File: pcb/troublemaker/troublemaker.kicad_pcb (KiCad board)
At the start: 2 copper layers, 419 x 394 mm, 116 parts, among them IC1 TEENSY_4.1, J1 neopixel_data_RPI19_GPIO10, J2 taptempo_led_RPI16_GPIO23, J3 5V_RPI2_OR_4, J4 GND_RPI34, J5 Conn_01x12, SW1 sw_eq2, SW10 sw_grain_playback, SW11 btn_sampler_stop, SW2 sw_eq1, SW3 sw_sub, SW4 sw_bass, SW5 sw_mid, SW6 sw_high, SW7 btn_delay_taptempo, SW8 sw_delay_type, SW9 sw_grain_type, U1 RASPBERRY_PI_4B_4GB, U2 CD74HC4067M, U3 CD74HC4067M, U4 CD74HC4067M, U5 CD74HC4067M, U6 CD74HC4067M

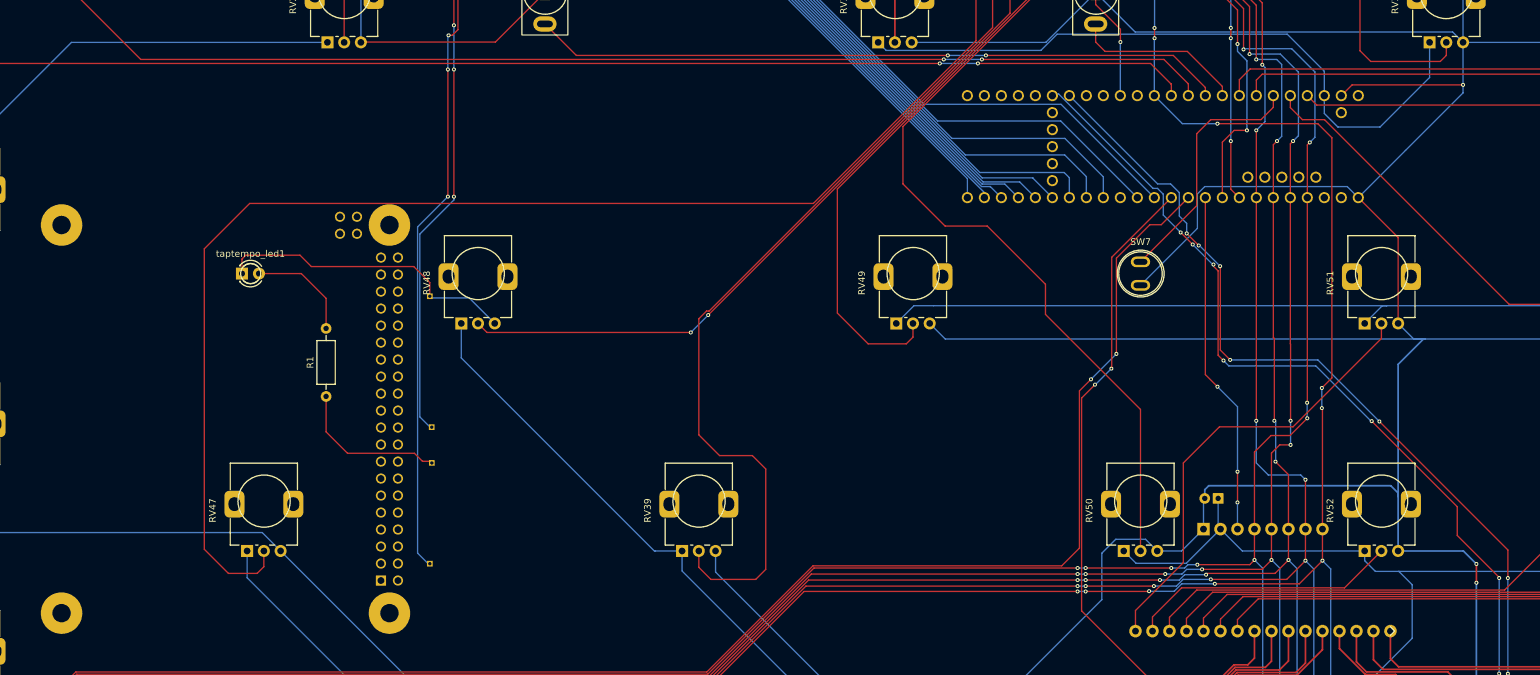
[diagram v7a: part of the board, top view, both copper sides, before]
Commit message: Fixed DRC errors
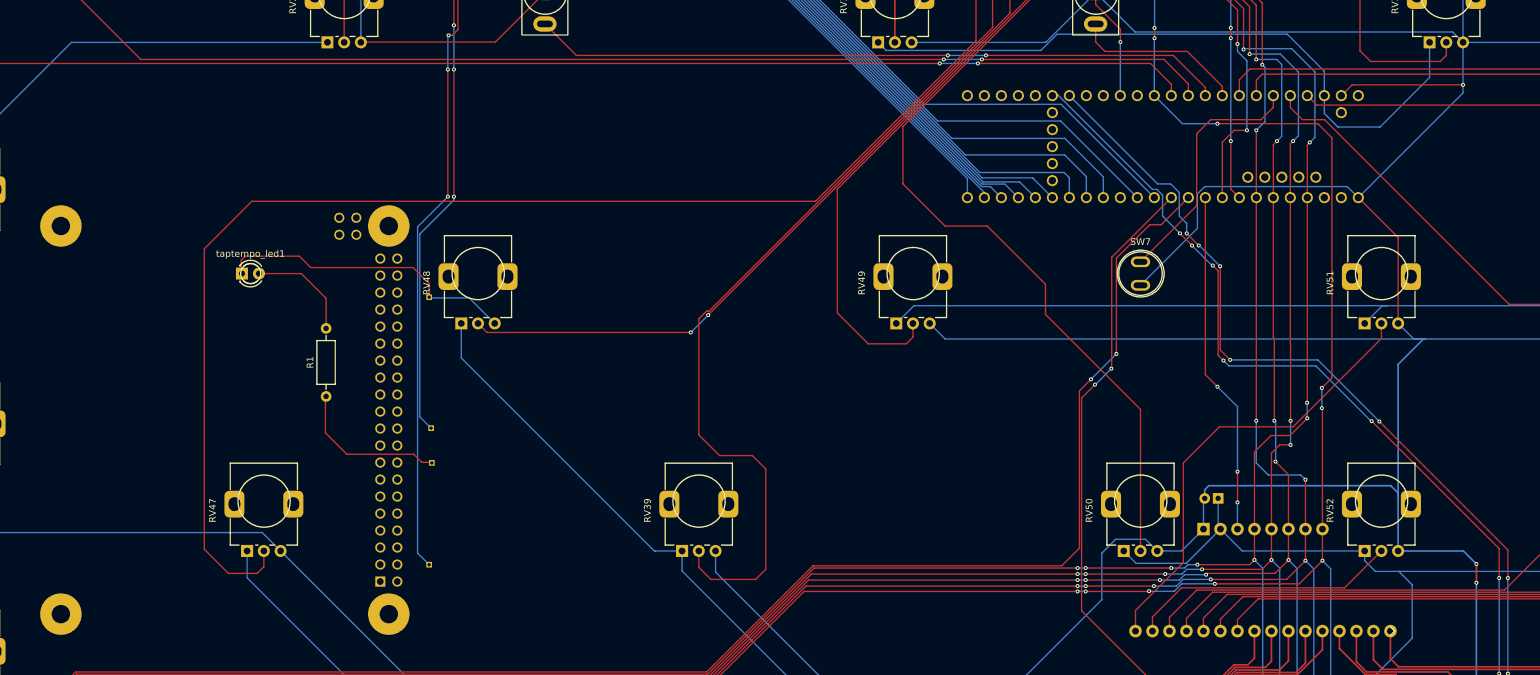
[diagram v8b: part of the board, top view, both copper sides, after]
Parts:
- moved U1 0.18 mm to (143.7, 233.6)
- moved J1 0.18 mm to (174.5, 244.8)
- moved J4 0.18 mm to (174.2, 225.2)
- moved J3 0.18 mm to (174.2, 265.2)
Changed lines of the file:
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@@
 	(footprint "Connector_PinHeader_1.00mm:PinHeader_1x01_P1.00mm_Vertical"
 		(layer "B.Cu")
-		(at 174.587699 244.652048 90)
+		(at 174.487699 244.8 90)
 		(descr "Through hole straight pin header, 1x01, 1.00mm pitch, single row")
 		(tags "Through hole pin header THT 1x01 1.00mm single row")
@@
 	(footprint "Connector_PinHeader_1.00mm:PinHeader_1x01_P1.00mm_Vertical"
 		(layer "B.Cu")
-		(at 174.300199 225.08525 90)
+		(at 174.200199 225.233202 90)
 		(descr "Through hole straight pin header, 1x01, 1.00mm pitch, single row")
 		(tags "Through hole pin header THT 1x01 1.00mm single row")
@@
 	(footprint "RASPBERRY_PI_4B_4GB:MODULE_RASPBERRY_PI_4B_4GB"
 		(layer "B.Cu")
-		(at 143.77 233.442048 90)
+		(at 143.67 233.59 90)
 		(property "Reference" "U1"
 			(at -39.575 29.635 -90)
@@
 	(footprint "Connector_PinHeader_1.00mm:PinHeader_1x01_P1.00mm_Vertical"
 		(layer "B.Cu")
-		(at 174.3 265.052048 90)
+		(at 174.2 265.2 90)
 		(descr "Through hole straight pin header, 1x01, 1.00mm pitch, single row")
 		(tags "Through hole pin header THT 1x01 1.00mm single row")
@@
 	)
 	(gr_text "USB C POWER THIS SIDE"
-		(at 113.800199 266.68525 -90)
+		(at 113.700199 266.833202 -90)
 		(layer "B.Fab")
 		(effects
@@
 	)
 	(segment
-		(start 156.6 220.652048)
-		(end 171.9 220.652048)
+		(start 156.5 220.8)
+		(end 171.8 220.8)
 		(width 0.2)
 		(layer "F.Cu")
@@
 	)
 	(segment
-		(start 146.225 219.527048)
-		(end 146.8 218.952048)
+		(start 146.125 219.675)
+		(end 146.7 219.1)
 		(width 0.2)
 		(layer "F.Cu")
@@
 	)
 	(segment
-		(start 146.225 221.452048)
-		(end 146.225 219.527048)
+		(start 146.125 221.6)
+		(end 146.125 219.675)
 		(width 0.2)
 		(layer "F.Cu")
@@
 	)
 	(segment
-		(start 154.9 218.952048)
-		(end 156.6 220.652048)
+		(start 154.8 219.1)
+		(end 156.5 220.8)
 		(width 0.2)
 		(layer "F.Cu")
@@
 	)
 	(segment
-		(start 146.8 218.952048)
-		(end 154.9 218.952048)
+		(start 146.7 219.1)
+		(end 154.8 219.1)
 		(width 0.2)
 		(layer "F.Cu")
@@
 	)
 	(segment
-		(start 174.300199 223.052247)
-		(end 174.300199 225.08525)
+		(start 174.200199 223.200199)
+		(end 174.200199 225.233202)
 		(width 0.2)
 		(layer "F.Cu")
@@
 	)
 	(segment
-		(start 171.9 220.652048)
-		(end 174.300199 223.052247)
+		(start 171.8 220.8)
+		(end 174.200199 223.200199)
 		(width 0.2)
 		(layer "F.Cu")
@@
 	)
 	(segment
+		(start 255.917753 186.917753)
+		(end 255.917753 172.017753)
+		(width 0.2)
+		(layer "F.Cu")
+		(net 30)
+	)
+	(segment
 		(start 255.87 167.17)
 		(end 255.87 164.63)
@@
 	)
 	(segment
-		(start 144.2 266.5)
-		(end 140.6 262.9)
+		(start 149.5 263.15)
+		(end 149.5 265.5)
 		(width 0.2)
 		(layer "F.Cu")
@@
 	)
 	(segment
-		(start 148.5 266.5)
-		(end 144.2 266.5)
+		(start 140.6 218)
+		(end 147.7 210.9)
 		(width 0.2)
 		(layer "F.Cu")
@@
 	)
 	(segment
-		(start 231.617753 211.217753)
+		(start 231.935506 210.9)
 		(end 255.917753 186.917753)
 		(width 0.2)
@@
 	)
 	(segment
-		(start 140.6 262.9)
-		(end 140.6 218)
+		(start 144.2 266.5)
+		(end 140.6 262.9)
 		(width 0.2)
 		(layer "F.Cu")
@@
 	)
 	(segment
-		(start 149.5 265.5)
-		(end 148.5 266.5)
+		(start 148.5 266.5)
+		(end 144.2 266.5)
 		(width 0.2)
 		(layer "F.Cu")
@@
 	)
 	(segment
-		(start 255.9 167.2)
-		(end 255.87 167.17)
-		(width 0.256)
+		(start 147.7 210.9)
+		(end 231.935506 210.9)
+		(width 0.2)
 		(layer "F.Cu")
 		(net 30)
@@
 	)
 	(segment
-		(start 147.382247 211.217753)
-		(end 231.617753 211.217753)
-		(width 0.2)
-		(layer "F.Cu")
-		(net 30)
-	)
-	(segment
-		(start 255.9 167.3)
-		(end 255.9 167.2)
+		(start 255.9 167.2)
+		(end 255.87 167.17)
 		(width 0.256)
 		(layer "F.Cu")
@@
 	)
 	(segment
-		(start 140.6 218)
-		(end 147.382247 211.217753)
+		(start 149.5 265.5)
+		(end 148.5 266.5)
 		(width 0.2)
 		(layer "F.Cu")
@@
 	)
 	(segment
-		(start 149.5 263.15)
-		(end 149.5 265.5)
-		(width 0.2)
+		(start 255.9 167.3)
+		(end 255.9 167.2)
+		(width 0.256)
 		(layer "F.Cu")
 		(net 30)
 	)
 	(segment
-		(start 255.917753 186.917753)
-		(end 255.917753 172.017753)
+		(start 140.6 262.9)
+		(end 140.6 218)
 		(width 0.2)
 		(layer "F.Cu")
@@
 	)
 	(segment
+		(start 334.1 262.8)
+		(end 334.1 267.2)
+		(width 0.2)
+		(layer "F.Cu")
+		(net 113)
+	)
+	(segment
 		(start 292.1 233.9)
 		(end 292.1 221.3)
@@
 	)
 	(segment
-		(start 334.1 267.1)
-		(end 334.1 267.2)
-		(width 0.2)
-		(layer "F.Cu")
-		(net 113)
-	)
-	(segment
 		(start 368.0275 315.4)
 		(end 334.1 281.4725)
@@
 	)
 	(segment
-		(start 315.05 243.75)
-		(end 327.834926 256.534926)
+		(start 286.4 215.7)
+		(end 288.2 217.5)
 		(width 0.2)
 		(layer "F.Cu")
@@
 	)
 	(segment
-		(start 286.5 215.552048)
-		(end 288.3 217.352048)
+		(start 315.05 243.75)
+		(end 334.1 262.8)
 		(width 0.2)
 		(layer "F.Cu")
@@
 		(net 113)
 	)
-	(segment
-		(start 327.834926 256.534926)
-		(end 327.834926 260.834926)
-		(width 0.2)
-		(layer "F.Cu")
-		(net 113)
-	)
-	(segment
-		(start 327.834926 260.834926)
-		(end 334.1 267.1)
-		(width 0.2)
-		(layer "F.Cu")
-		(net 113)
-	)
 	(via
-		(at 291.4 220.352048)
+		(at 291.3 220.5)
 		(size 0.6)
 		(drill 0.3)
@@
 	)
 	(via
-		(at 288.3 217.352048)
+		(at 288.2 217.5)
 		(size 0.6)
 		(drill 0.3)
@@
 	)
 	(via
-		(at 286.5 215.552048)
+		(at 286.4 215.7)
 		(size 0.6)
 		(drill 0.3)
@@
 	)
 	(segment
-		(start 291.3 220.352048)
-		(end 291.4 220.352048)
+		(start 291.2 220.5)
+		(end 291.3 220.5)
 		(width 0.2)
 		(layer "B.Cu")
@@
 	)
 	(segment
-		(start 288.3 217.352048)
-		(end 291.3 220.352048)
+		(start 288.2 217.5)
+		(end 291.2 220.5)
 		(width 0.2)
 		(layer "B.Cu")
@@
 	)
 	(segment
-		(start 282.375903 208.969548)
-		(end 283.039097 208.969548)
+		(start 282.275903 209.1175)
+		(end 282.939097 209.1175)
 		(width 0.2)
 		(layer "B.Cu")
@@
 	)
 	(segment
-		(start 283.039097 208.969548)
-		(end 283.9 209.830451)
+		(start 282.939097 209.1175)
+		(end 283.8 209.978403)
 		(width 0.2)
 		(layer "B.Cu")
@@
 	)
 	(segment
-		(start 283.9 212.952048)
-		(end 286.5 215.552048)
+		(start 283.8 213.1)
+		(end 286.4 215.7)
 		(width 0.2)
 		(layer "B.Cu")
@@
 	)
 	(segment
-		(start 283.9 209.830451)
-		(end 283.9 212.952048)
+		(start 283.8 209.978403)
+		(end 283.8 213.1)
 		(width 0.2)
 		(layer "B.Cu")
@@
 	)
 	(segment
-		(start 267.33 194.862048)
-		(end 268.268403 194.862048)
+		(start 267.23 195.01)
+		(end 268.168403 195.01)
 		(width 0.2)
 		(layer "B.Cu")
@@
 	)
 	(segment
-		(start 268.268403 194.862048)
-		(end 282.375903 208.969548)
+		(start 268.168403 195.01)
+		(end 282.275903 209.1175)
 		(width 0.2)
 		(layer "B.Cu")
@@
 	)
 	(segment
-		(start 162 248.552048)
-		(end 172 248.552048)
+		(start 161.9 248.7)
+		(end 171.9 248.7)
 		(width 0.2)
 		(layer "F.Cu")
@@
 	)
 	(segment
-		(start 158.8 245.352048)
-		(end 162 248.552048)
+		(start 158.7 245.5)
+		(end 161.9 248.7)
 		(width 0.2)
 		(layer "F.Cu")
@@
 	)
 	(segment
-		(start 172 248.552048)
-		(end 173.2 249.752048)
+		(start 171.9 248.7)
+		(end 173.1 249.9)
 		(width 0.2)
 		(layer "F.Cu")
@@
 	)
 	(segment
-		(start 158.8 239.812048)
-		(end 158.8 245.352048)
+		(start 158.7 239.96)
+		(end 158.7 245.5)
 		(width 0.2)
 		(layer "F.Cu")
@@
 	)
 	(segment
-		(start 173.2 249.752048)
-		(end 174.6 249.752048)
+		(start 173.1 249.9)
+		(end 174.5 249.9)
 		(width 0.2)
 		(layer "F.Cu")
